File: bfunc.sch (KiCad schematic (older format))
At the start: 18 parts

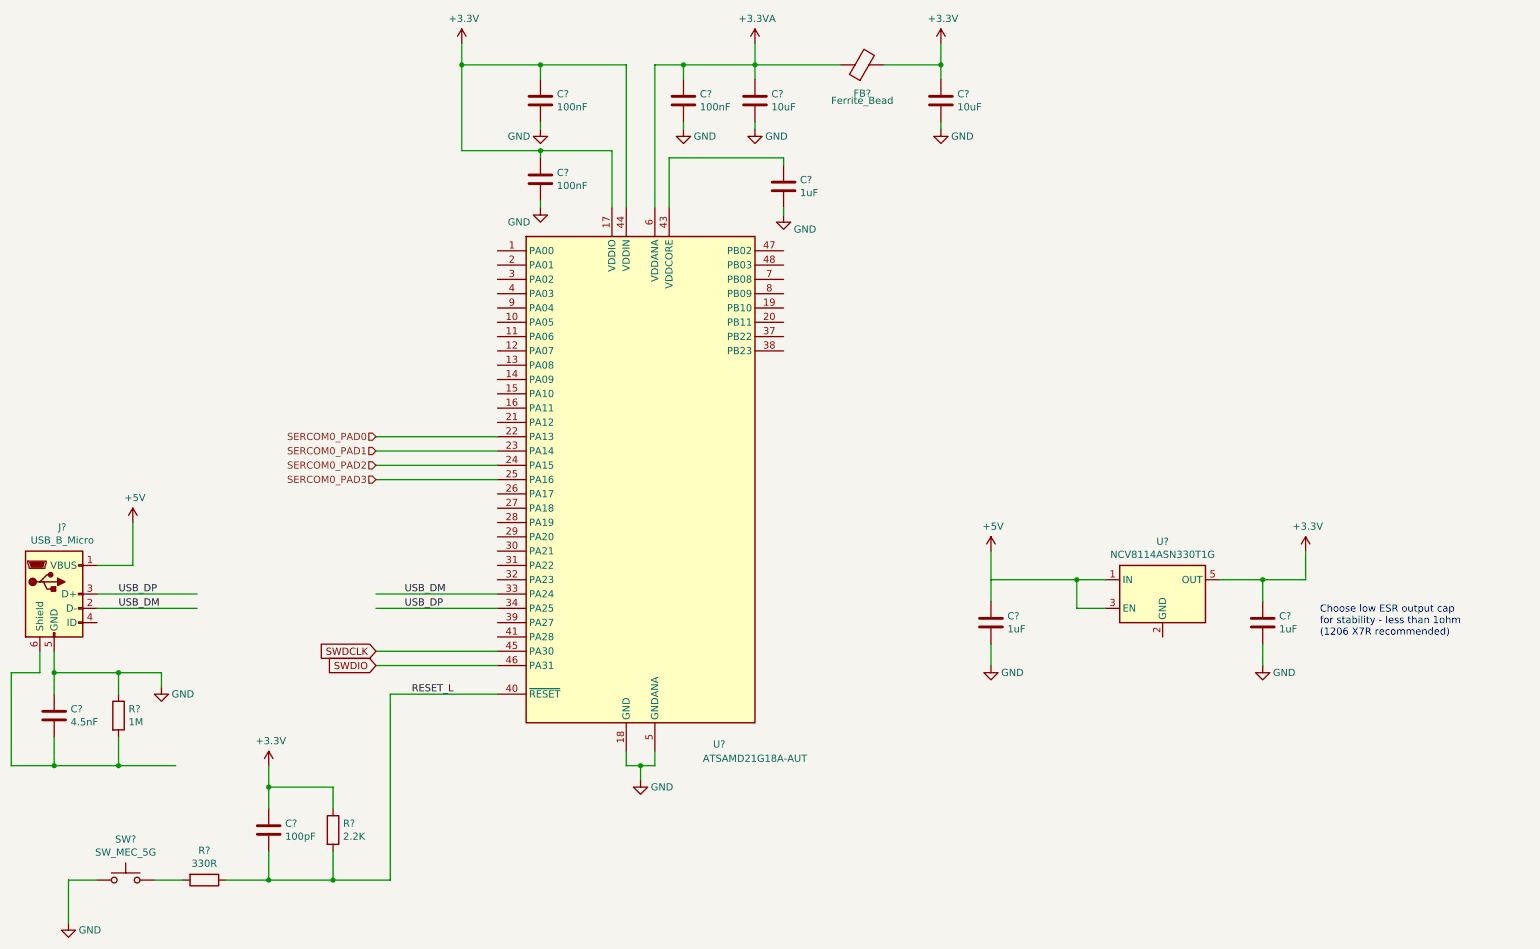
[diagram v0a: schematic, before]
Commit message: Broke cmpts into hierarchical design; swapped over to STM32 MCU (better USB reference examples, better toolchain support for my shitty old Mac)
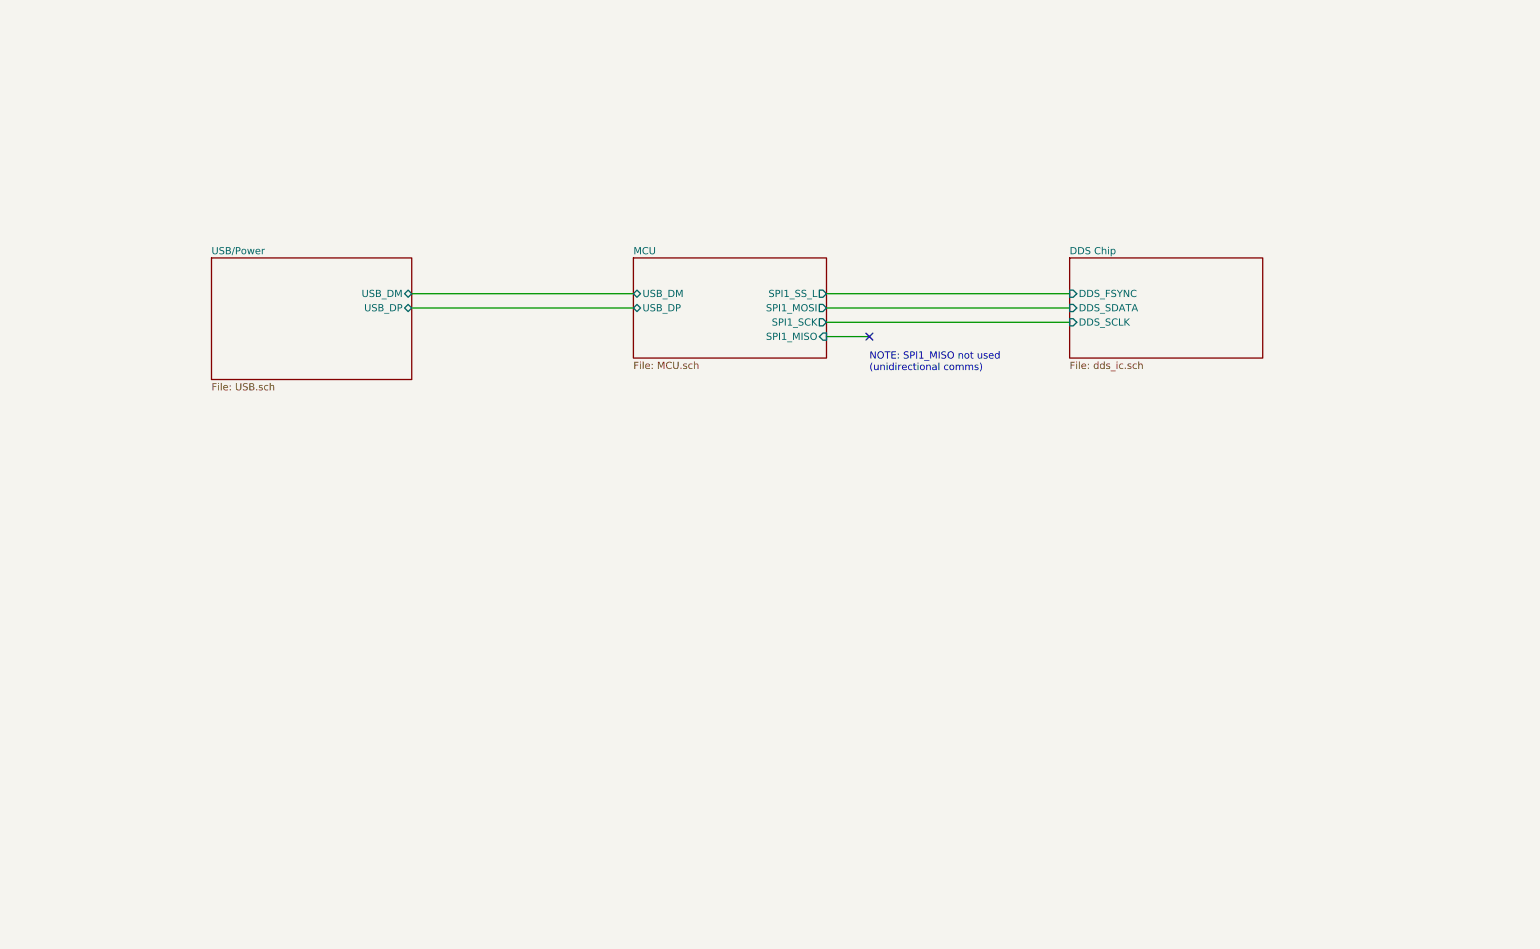
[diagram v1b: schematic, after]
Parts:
- removed C? (x3): 100nF, symbol Device:C
- removed C? (x3): 1uF, symbol Device:C
- removed C? (x2): 10uF, symbol Device:C
- removed C?: 100pF, symbol Device:C
- removed C?: 4.5nF, symbol Device:C
- removed FB?: Ferrite_Bead, symbol Device:Ferrite_Bead
- removed J?: USB_B_Micro, symbol Connector:USB_B_Micro
- removed R?: 2.2K, symbol Device:R
- removed R?: 330R, symbol Device:R
- removed R?: 1M, symbol Device:R
- removed SW?: SW_MEC_5G, symbol Switch:SW_MEC_5G
- removed U?: ATSAMD21G18A-AUT, Package_QFP:TQFP-48_7x7mm_P0.5mm, symbol MCU_Microchip_SAMD:ATSAMD21G18A-AUT
- removed U?: NCV8114ASN330T1G, Package_TO_SOT_SMD:TSOT-23-5, symbol Regulator_Linear:NCV8114ASN330T1G
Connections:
- net labels removed: +3.3V, +3.3VA, +5V, GND, RESET_L, SERCOM0_PAD0, SERCOM0_PAD1, SERCOM0_PAD2, SERCOM0_PAD3, SWDCLK, SWDIO, USB_DM, USB_DP
- wire segments 86 -> 6
- no-connect marks 0 -> 1
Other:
- note added: "NOTE: SPI1_MISO not used\n(unidirectional comms)"
- note removed: "Choose low ESR output cap \nfor stability - less than 1ohm\n(1206 X7R recommended)"
